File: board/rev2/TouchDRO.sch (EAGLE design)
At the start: 23 parts, among them U2 VREG_33, U3 VREG_5

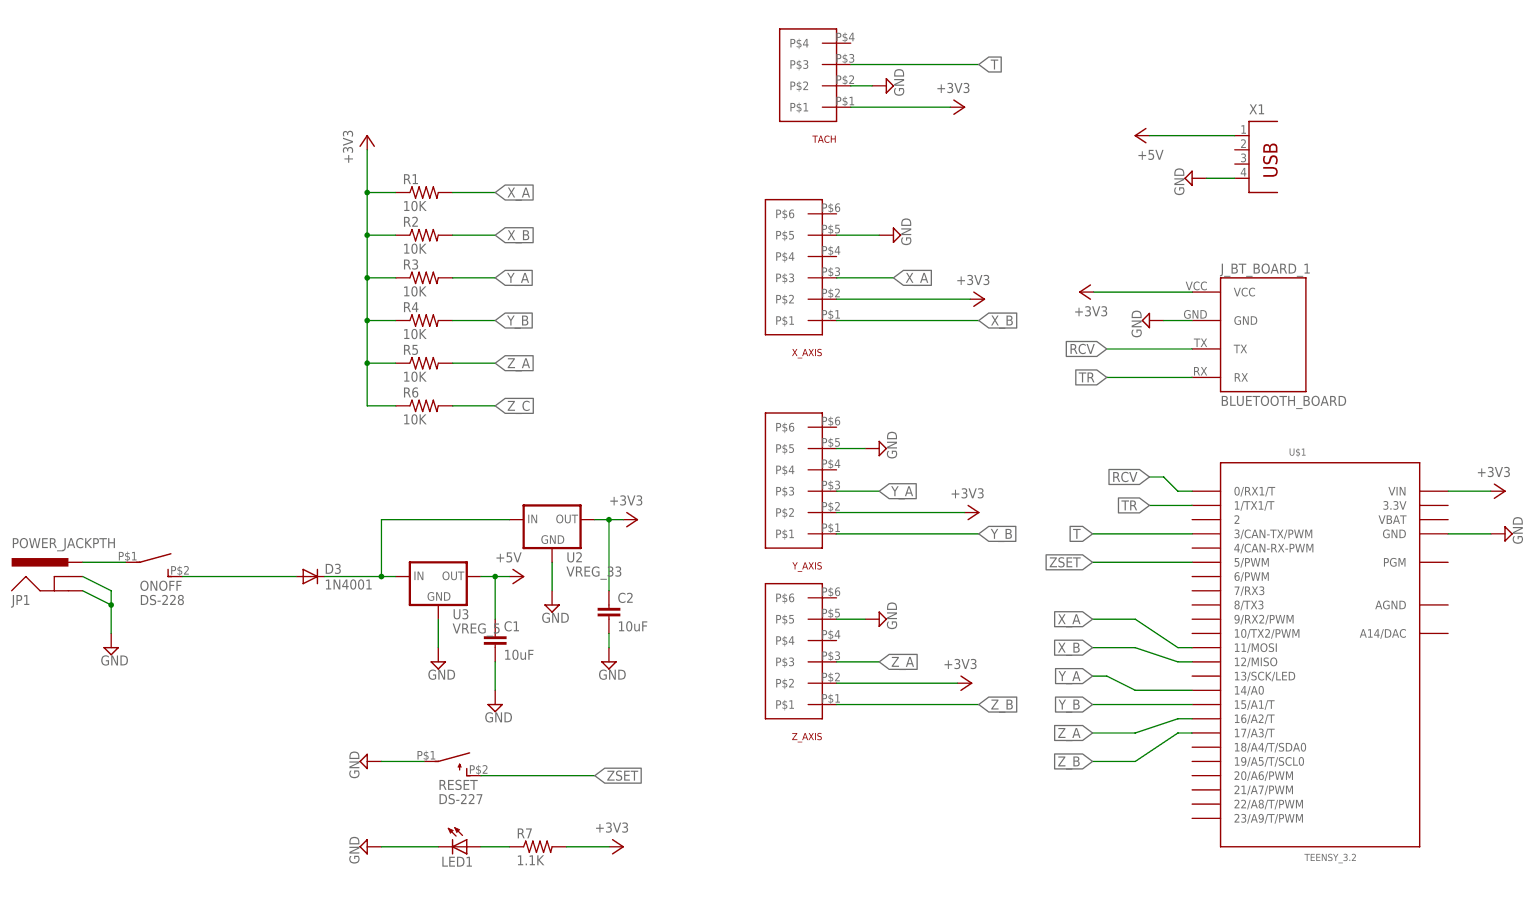
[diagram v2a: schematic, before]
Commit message: added usb type-a connector. add power supply cap.
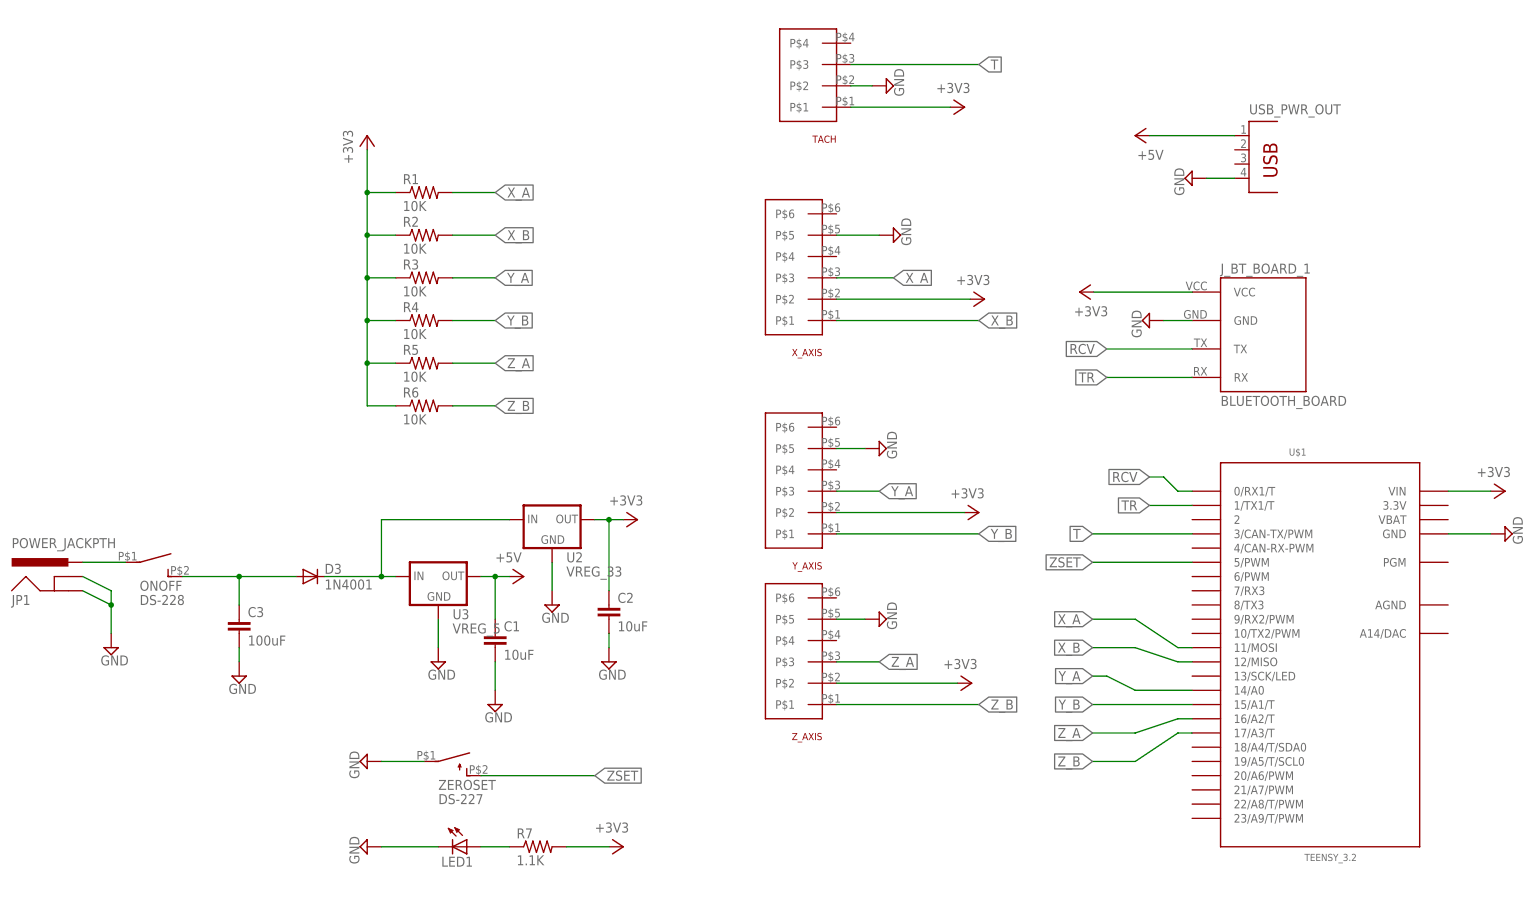
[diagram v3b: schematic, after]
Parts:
- removed X1: (no value), con-berg:PN87520
- added C3: 100uF, SparkFun-Passives:CAPEZ
- added USB_PWR_OUT: (no value), USB:USBTYPEA
- renumbered RESET to ZEROSET
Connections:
- removed net Z_C: R6.2
- net +5V: now also USB_PWR_OUT.1; no longer X1.1
- net GND: now also C3.2, USB_PWR_OUT.4; no longer X1.4
- net ONOFF: now also C3.1
- net Z_B: now also R6.2
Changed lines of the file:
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@@
 <part name="R5" library="SparkFun-Passives" deviceset="RESISTOR" device="EZ" value="10K"/>
 <part name="R6" library="SparkFun-Passives" deviceset="RESISTOR" device="EZ" value="10K"/>
-<part name="RESET" library="Switches" deviceset="DS-227" device=""/>
+<part name="ZEROSET" library="Switches" deviceset="DS-227" device=""/>
 <part name="ONOFF" library="Switches" deviceset="DS-228" device=""/>
-<part name="X1" library="con-berg" deviceset="PN87520" device=""/>
 <part name="U2" library="regulators" deviceset="VREG_33" device=""/>
 <part name="U3" library="regulators" deviceset="VREG_5" device=""/>
@@
 <part name="+3V7" library="supply1" deviceset="+3V3" device=""/>
 <part name="R7" library="SparkFun-Passives" deviceset="RESISTOR" device="EZ" value="1.1K"/>
+<part name="USB_PWR_OUT" library="USB" deviceset="USBTYPEA" device=""/>
+<part name="C3" library="SparkFun-Passives" deviceset="CAP" device="EZ" value="100uF"/>
+<part name="SUPPLY8" library="supply2" deviceset="GND" device=""/>
 </parts>
 <sheets>
@@
 <instance part="R5" gate="G$1" x="-81.28" y="33.02"/>
 <instance part="R6" gate="G$1" x="-81.28" y="25.4"/>
-<instance part="RESET" gate="G$1" x="-76.2" y="-38.1" rot="R270"/>
+<instance part="ZEROSET" gate="G$1" x="-76.2" y="-38.1" rot="R270"/>
 <instance part="ONOFF" gate="G$1" x="-129.54" y="-2.54" rot="R270"/>
-<instance part="X1" gate="G$1" x="66.04" y="68.58"/>
 <instance part="U2" gate="G$1" x="-58.42" y="5.08"/>
 <instance part="U3" gate="G$1" x="-78.74" y="-5.08"/>
@@
 <instance part="+3V7" gate="G$1" x="-45.72" y="-53.34" rot="R270"/>
 <instance part="R7" gate="G$1" x="-60.96" y="-53.34"/>
+<instance part="USB_PWR_OUT" gate="G$1" x="66.04" y="68.58"/>
+<instance part="C3" gate="G$1" x="-114.3" y="-15.24"/>
+<instance part="SUPPLY8" gate="GND" x="-114.3" y="-22.86"/>
 </instances>
 <busses>
@@
 <segment>
 <pinref part="SUPPLY3" gate="GND" pin="GND"/>
-<pinref part="RESET" gate="G$1" pin="P"/>
+<pinref part="ZEROSET" gate="G$1" pin="P"/>
 <wire x1="-88.9" y1="-38.1" x2="-81.28" y2="-38.1" width="0.1524" layer="91"/>
 </segment>
 <segment>
-<pinref part="X1" gate="G$1" pin="4"/>
 <wire x1="63.5" y1="66.04" x2="58.42" y2="66.04" width="0.1524" layer="91"/>
 <pinref part="SUPPLY20" gate="GND" pin="GND"/>
+<pinref part="USB_PWR_OUT" gate="G$1" pin="4"/>
 </segment>
 <segment>
@@
 <pinref part="LED1" gate="G$1" pin="C"/>
 <wire x1="-88.9" y1="-53.34" x2="-78.74" y2="-53.34" width="0.1524" layer="91"/>
+</segment>
+<segment>
+<pinref part="C3" gate="G$1" pin="2"/>
+<pinref part="SUPPLY8" gate="GND" pin="GND"/>
+<wire x1="-114.3" y1="-17.78" x2="-114.3" y2="-20.32" width="0.1524" layer="91"/>
 </segment>
 </net>
@@
 <label x="38.1" y="-38.1" size="1.778" layer="95" rot="R180" xref="yes"/>
 </segment>
+<segment>
+<wire x1="-68.58" y1="25.4" x2="-76.2" y2="25.4" width="0.1524" layer="91"/>
+<label x="-68.58" y="25.4" size="1.778" layer="95" xref="yes"/>
+<pinref part="R6" gate="G$1" pin="2"/>
+</segment>
 </net>
 <net name="Y_A" class="0">
@@
 <segment>
 <pinref part="D3" gate="G$1" pin="A"/>
-<wire x1="-124.46" y1="-5.08" x2="-104.14" y2="-5.08" width="0.1524" layer="91"/>
+<wire x1="-124.46" y1="-5.08" x2="-114.3" y2="-5.08" width="0.1524" layer="91"/>
 <pinref part="ONOFF" gate="G$1" pin="S"/>
+<pinref part="C3" gate="G$1" pin="1"/>
+<wire x1="-114.3" y1="-5.08" x2="-104.14" y2="-5.08" width="0.1524" layer="91"/>
+<wire x1="-114.3" y1="-10.16" x2="-114.3" y2="-5.08" width="0.1524" layer="91"/>
+<junction x="-114.3" y="-5.08"/>
 </segment>
 </net>
@@
 </segment>
 <segment>
-<pinref part="X1" gate="G$1" pin="1"/>
 <wire x1="48.26" y1="73.66" x2="63.5" y2="73.66" width="0.1524" layer="91"/>
 <pinref part="P+1" gate="1" pin="+5V"/>
+<pinref part="USB_PWR_OUT" gate="G$1" pin="1"/>
 </segment>
 </net>
@@
 </segment>
 </net>
-<net name="Z_C" class="0">
-<segment>
-<wire x1="-68.58" y1="25.4" x2="-76.2" y2="25.4" width="0.1524" layer="91"/>
-<label x="-68.58" y="25.4" size="1.778" layer="95" xref="yes"/>
-<pinref part="R6" gate="G$1" pin="2"/>
-</segment>
-</net>
 <net name="ZSET" class="0">
 <segment>
@@
 <wire x1="-71.12" y1="-40.64" x2="-50.8" y2="-40.64" width="0.1524" layer="91"/>
 <label x="-50.8" y="-40.64" size="1.778" layer="95" xref="yes"/>
-<pinref part="RESET" gate="G$1" pin="S"/>
-</segment>
-</net>
+<pinref part="ZEROSET" gate="G$1" pin="S"/>
+</segment>
+</net>
